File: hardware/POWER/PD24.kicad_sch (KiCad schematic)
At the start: 5 parts, among them J1 USB_C_Receptacle_USB2.0_16P, J2 Conn_01x02_Pin, J4 Conn_01x08_Pin, J5 Conn_01x12_Pin

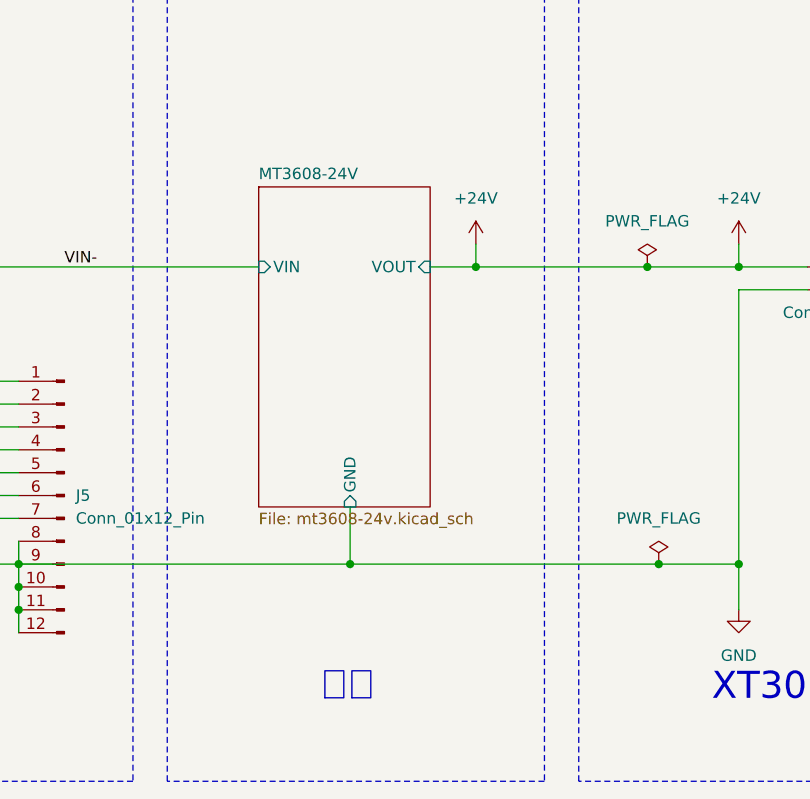
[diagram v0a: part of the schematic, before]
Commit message: 硬件v1调整布局将肖特基二极管放置正面，便于贴片
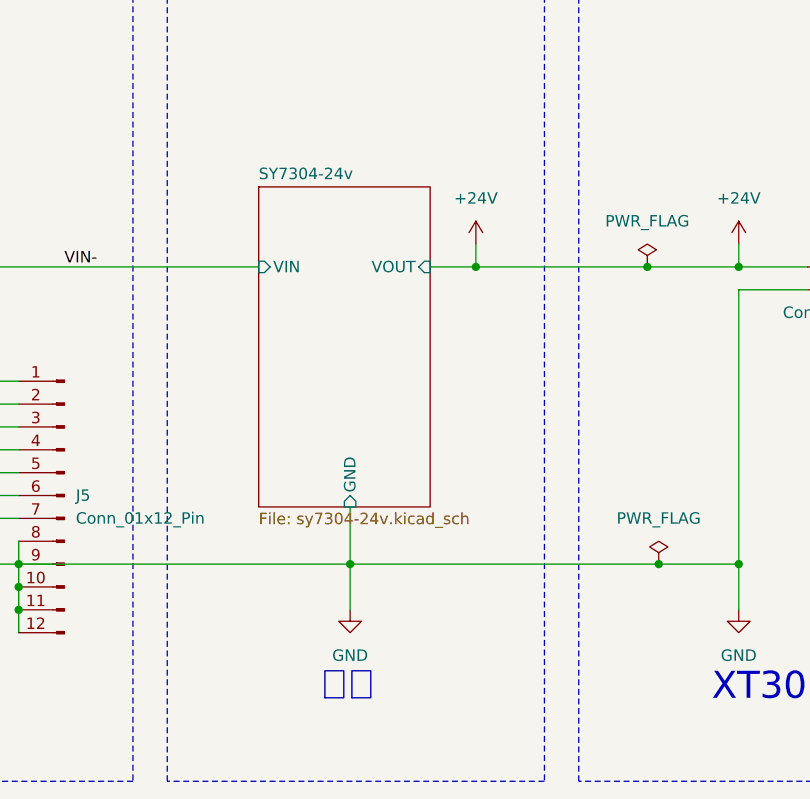
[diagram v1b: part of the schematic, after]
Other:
- removed sheet MT3608-24V
- added sheet SY7304-24v (sy7304-24v.kicad_sch)
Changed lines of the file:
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@@
+	(wire
+		(pts
+			(xy 200.66 116.84) (xy 200.66 121.92)
+		)
+		(stroke
+			(width 0)
+			(type default)
+		)
+	)
 	(wire
 		(pts
@@
 	)
 	(symbol
+		(lib_id "power:GND")
+		(at 200.66 121.92 0)
+		(unit 1)
+		(exclude_from_sim no)
+		(in_bom yes)
+		(on_board yes)
+		(dnp no)
+		(fields_autoplaced yes)
+		(property "Reference" "#PWR05"
+			(at 200.66 128.27 0)
+			(effects
+				(font
+					(size 1.27 1.27)
+				)
+				(hide yes)
+			)
+		)
+		(property "Value" "GND"
+			(at 200.66 127 0)
+			(effects
+				(font
+					(size 1.27 1.27)
+				)
+			)
+		)
+		(property "Footprint" ""
+			(at 200.66 121.92 0)
+			(effects
+				(font
+					(size 1.27 1.27)
+				)
+				(hide yes)
+			)
+		)
+		(property "Datasheet" ""
+			(at 200.66 121.92 0)
+			(effects
+				(font
+					(size 1.27 1.27)
+				)
+				(hide yes)
+			)
+		)
+		(property "Description" "Power symbol creates a global label with name \"GND\" , ground"
+			(at 200.66 121.92 0)
+			(effects
+				(font
+					(size 1.27 1.27)
+				)
+				(hide yes)
+			)
+		)
+		(pin "1"
+		)
+		(instances
+			(project "PD24"
+				(path "/10096dd5-e34a-417b-937d-8bf7da4f4410"
+					(reference "#PWR05")
+					(unit 1)
+				)
+			)
+		)
+	)
+	(symbol
 		(lib_id "power:+3V3")
 		(at 214.63 81.28 0)
@@
 			(color 0 0 0 0.0000)
 		)
-		(property "Sheetname" "MT3608-24V"
+		(property "Sheetname" "SY7304-24v"
 			(at 190.5 74.2184 0)
 			(effects
@@
 			)
 		)
-		(property "Sheetfile" "mt3608-24v.kicad_sch"
+		(property "Sheetfile" "sy7304-24v.kicad_sch"
 			(at 190.5 111.0746 0)
 			(effects
@@
 				)
 				(justify left top)
+			)
+		)
+		(pin "VIN" input
+			(at 190.5 83.82 180)
+			(effects
+				(font
+					(size 1.27 1.27)
+				)
+				(justify left)
 			)
 		)
@@
 			(effects
 				(font
-					(size 1.27 1.27)
-				)
-				(justify left)
-			)
-		)
-		(pin "VIN" input
-			(at 190.5 83.82 180)
-			(effects
-				(font

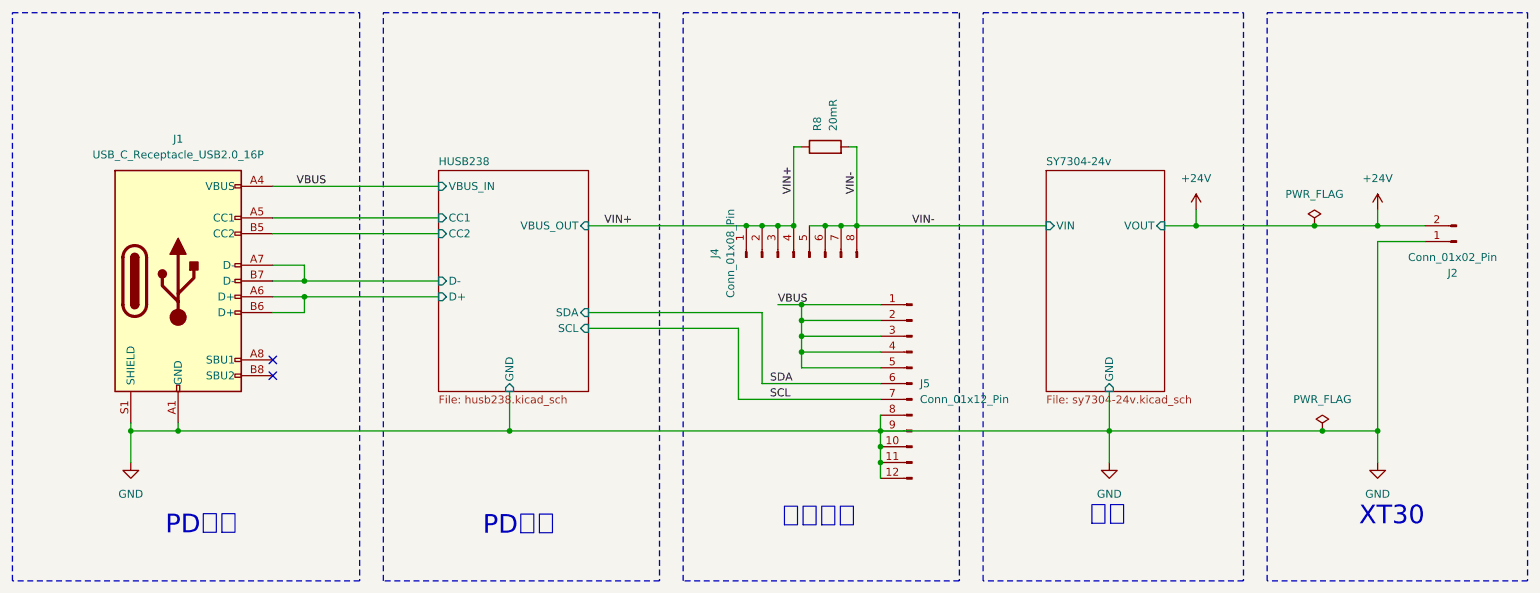
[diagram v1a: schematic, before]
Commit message: 更换升压方案为同步整流，较大降低了升压电路的发热量，将acc和ldo放在电源板上
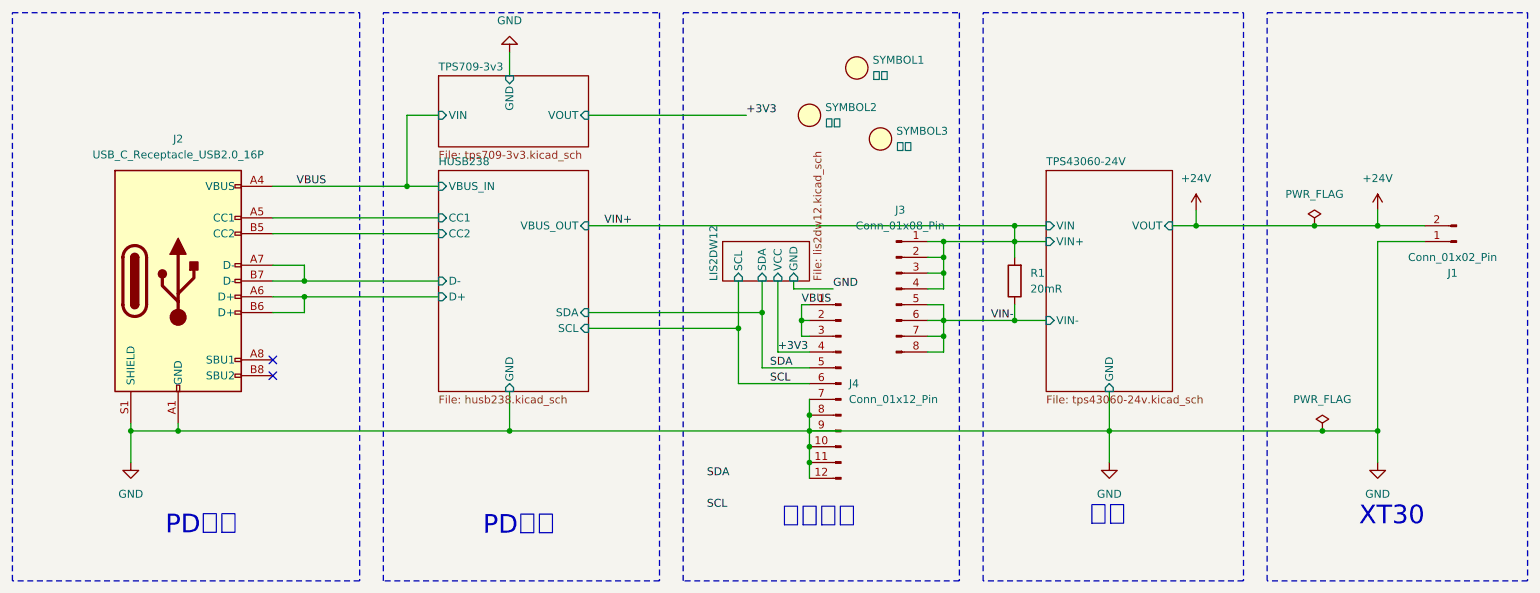
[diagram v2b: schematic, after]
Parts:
- removed R8: 20mR, Resistor_SMD:R_1206_3216Metric, symbol Device:R
- added R1: 20mR, Resistor_SMD:R_1206_3216Metric, symbol Device:R
- added SYMBOL1: 符号, Symbol:KiCad-Logo2_5mm_Copper, symbol my_symbol:symbol
- added SYMBOL2: 符号, Symbol:OSHW-Symbol_8.9x8mm_SilkScreen, symbol my_symbol:symbol
- added SYMBOL3: 符号, Symbol:ESD-Logo_6.6x6mm_SilkScreen, symbol my_symbol:symbol
- renumbered J2 to J1, J1 to J2, J4 to J3, J5 to J4
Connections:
- net GND: now also J4.7 (Pin_7)
- net SCL: now also J4.6 (Pin_6); no longer J4.7 (Pin_7)
- net SDA: now also J4.5 (Pin_5); no longer J4.6 (Pin_6)
- net VBUS: no longer J4.4 (Pin_4), J4.5 (Pin_5)
- net VIN+: now also R1.2
- net VIN-: now also R1.1
- new net +3V3: J4.4 (Pin_4)
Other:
- removed sheet SY7304-24v
- added sheet LIS2DW12 (lis2dw12.kicad_sch)
- added sheet TPS43060-24V (tps43060-24v.kicad_sch)
- added sheet TPS709-3v3 (tps709-3v3.kicad_sch)
- moved on the sheet: J3, J4

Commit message: 硬件版本v2，待验证
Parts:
- SYMBOL1, SYMBOL2, SYMBOL3: now left out of the parts list
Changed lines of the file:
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@@
 		)
 	)
-	(label "SDA"
-		(at 135.89 124.46 0)
+	(label "VIN-"
+		(at 181.61 99.06 0)
 		(fields_autoplaced yes)
 		(effects
@@
 		)
 	)
-	(label "VIN-"
-		(at 181.61 99.06 0)
+	(label "+3V3"
+		(at 147.32 104.14 0)
 		(fields_autoplaced yes)
 		(effects
@@
 		)
 	)
-	(label "+3V3"
-		(at 147.32 104.14 0)
+	(label "SCL"
+		(at 146.05 109.22 0)
 		(fields_autoplaced yes)
 		(effects
@@
 		)
 	)
-	(label "SCL"
-		(at 146.05 109.22 0)
+	(label "VIN+"
+		(at 119.38 83.82 0)
 		(fields_autoplaced yes)
 		(effects
@@
 		)
 	)
-	(label "VIN+"
-		(at 119.38 83.82 0)
+	(label "VBUS"
+		(at 69.85 77.47 0)
 		(fields_autoplaced yes)
 		(effects
@@
 		)
 	)
-	(label "SCL"
-		(at 135.89 129.54 0)
+	(label "GND"
+		(at 156.21 93.98 0)
 		(fields_autoplaced yes)
 		(effects
@@
 		)
 	)
-	(label "VBUS"
-		(at 69.85 77.47 0)
+	(label "SDA"
+		(at 146.05 106.68 0)
 		(fields_autoplaced yes)
 		(effects
@@
 		)
 	)
-	(label "GND"
-		(at 156.21 93.98 0)
+	(label "+3V3"
+		(at 142.24 66.04 0)
 		(fields_autoplaced yes)
 		(effects
@@
 		)
 	)
-	(label "SDA"
-		(at 146.05 106.68 0)
-		(fields_autoplaced yes)
-		(effects
-			(font
-				(size 1.27 1.27)
-			)
-			(justify left bottom)
-		)
-	)
-	(label "+3V3"
-		(at 142.24 66.04 0)
-		(fields_autoplaced yes)
-		(effects
-			(font
-				(size 1.27 1.27)
-			)
-			(justify left bottom)
-		)
-	)
 	(symbol
 		(lib_id "Connector:USB_C_Receptacle_USB2.0_16P")
@@
 		(unit 1)
 		(exclude_from_sim no)
-		(in_bom yes)
+		(in_bom no)
 		(on_board yes)
 		(dnp no)
@@
 		(unit 1)
 		(exclude_from_sim no)
-		(in_bom yes)
+		(in_bom no)
 		(on_board yes)
 		(dnp no)
@@
 		(unit 1)
 		(exclude_from_sim no)
-		(in_bom yes)
-		(on_board yes)
-		(dnp no)
+		(in_bom no)
+		(on_board yes)
+		(dnp no)
